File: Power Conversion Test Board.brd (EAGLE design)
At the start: 136.7 x 125.3 mm, 49 parts, among them U1 LM2678, U2 LM2678

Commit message: minor changes
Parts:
- added U$11, U$12, U$6: ET60S, ET60S:ET60S
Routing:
- net +3.3V: track 38.8 -> 28.8 mm, vias 1 -> 0
- net +5V: track 133.5 -> 136.1 mm
- net 3.3VGND: track 186.6 -> 188.2 mm
- net +12V: track 142.7 -> 143.5 mm
- net 5VGND: track 103.2 -> 103.4 mm, vias 7 -> 6
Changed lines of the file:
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@@
 </element>
 <element name="U$2" library="PDB_PCB_connectors" package="PDB_PCB_2" value="PDB_PCB_CONNEC" x="0" y="0"/>
+<element name="U$6" library="ET60S" package="ET60S" value="ET60S" x="40.3606" y="36.6776" rot="R120"/>
+<element name="U$11" library="ET60S" package="ET60S" value="ET60S" x="108.4072" y="57.7088" rot="R240"/>
+<element name="U$12" library="ET60S" package="ET60S" value="ET60S" x="56.1848" y="106.0958"/>
 </elements>
 <signals>
@@
 <wire x1="76.282" y1="56.642" x2="75.858" y2="57.066" width="1.27" layer="16"/>
 <wire x1="70.104" y1="69.596" x2="68.326" y2="71.374" width="1.27" layer="1"/>
-<wire x1="49.022" y1="71.374" x2="49.022" y2="68.834" width="1.143" layer="1"/>
 <wire x1="49.784" y1="68.072" x2="49.784" y2="66.548" width="1.143" layer="16"/>
 <wire x1="51.054" y1="65.278" x2="49.784" y2="66.548" width="1.143" layer="16"/>
@@
 <contactref element="U$2" pad="+12V14"/>
 <contactref element="U$2" pad="+12V44"/>
+<wire x1="49.022" y1="68.834" x2="48.1076" y2="69.7484" width="1.016" layer="1"/>
+<wire x1="48.1076" y1="70.4596" x2="49.022" y2="71.374" width="1.016" layer="1"/>
+<wire x1="48.1076" y1="69.7484" x2="48.1076" y2="70.4596" width="1.016" layer="1"/>
 <wire x1="93.446040625" y1="116.670159375" x2="95.9860375" y2="116.670159375" width="0" layer="19" extent="1-1"/>
 <wire x1="95.9860375" y1="114.1301625" x2="95.9860375" y2="116.670159375" width="0" layer="19" extent="1-1"/>
@@
 <contactref element="J6" pad="P$1"/>
 <wire x1="65.614" y1="97.962" x2="65.614" y2="94.234" width="1.27" layer="1"/>
-<wire x1="63.754" y1="99.822" x2="33.528" y2="99.822" width="1.27" layer="1"/>
-<wire x1="33.528" y1="99.822" x2="24.13" y2="109.22" width="1.27" layer="1"/>
-<wire x1="24.13" y1="110.744" x2="24.13" y2="109.22" width="1.27" layer="1"/>
-<wire x1="65.614" y1="97.962" x2="63.754" y2="99.822" width="1.27" layer="1"/>
 <wire x1="65.614" y1="94.234" x2="65.614" y2="88.392" width="1.27" layer="1"/>
 <wire x1="65.614" y1="88.392" x2="65.614" y2="82.55" width="1.27" layer="1"/>
@@
 <wire x1="46.736" y1="64.77" x2="46.736" y2="64.516" width="1.143" layer="16"/>
 <wire x1="54.864" y1="56.388" x2="46.736" y2="64.516" width="1.143" layer="16"/>
+<wire x1="24.13" y1="110.744" x2="34.7472" y2="100.1268" width="2.54" layer="1"/>
+<wire x1="65.614" y1="97.5556" x2="65.614" y2="94.234" width="2.54" layer="1"/>
+<wire x1="34.7472" y1="100.1268" x2="63.0428" y2="100.1268" width="2.54" layer="1"/>
+<wire x1="63.0428" y1="100.1268" x2="65.614" y2="97.5556" width="2.54" layer="1"/>
 </signal>
 <signal name="N$1">
@@
 <wire x1="56.642" y1="25.146" x2="49.022" y2="17.526" width="1.143" layer="16"/>
 <wire x1="49.022" y1="17.526" x2="49.022" y2="13.97" width="1.143" layer="16"/>
-<wire x1="69.85" y1="28.829" x2="69.85" y2="21.844" width="1.143" layer="1"/>
-<via x="69.85" y="28.829" extent="1-16" drill="0.6"/>
-<wire x1="69.85" y1="28.829" x2="69.547" y2="29.132" width="1.143" layer="16"/>
-<wire x1="69.547" y1="29.132" x2="67.024" y2="29.132" width="1.143" layer="16"/>
 </signal>
 <signal name="N$2">
@@
 <wire x1="94.0562" y1="64.3128" x2="99.008" y2="69.2646" width="0.889" layer="16"/>
 <wire x1="99.008" y1="74.168" x2="99.008" y2="77.2148" width="0.889" layer="16"/>
-<wire x1="101.766" y1="79.9728" x2="101.766" y2="88.138" width="0.889" layer="16"/>
-<wire x1="99.008" y1="77.2148" x2="101.766" y2="79.9728" width="0.889" layer="16"/>
+<wire x1="99.008" y1="77.2148" x2="102.362" y2="80.5688" width="1.016" layer="16"/>
+<wire x1="102.362" y1="87.542" x2="101.766" y2="88.138" width="1.016" layer="16"/>
+<wire x1="102.362" y1="80.5688" x2="102.362" y2="87.542" width="1.016" layer="16"/>
 </signal>
 <signal name="3.3VGND">
@@
 <wire x1="91.7448" y1="78.74" x2="93.091" y2="80.0862" width="0.889" layer="16"/>
 <via x="93.091" y="80.0862" extent="1-16" drill="0.6"/>
-<wire x1="93.091" y1="80.0862" x2="93.7142" y2="80.0862" width="0.889" layer="1"/>
-<wire x1="93.7142" y1="80.0862" x2="101.702" y2="88.074" width="0.889" layer="1"/>
 <wire x1="106.188" y1="76.453" x2="106.188" y2="87.3346" width="0.889" layer="16"/>
 <wire x1="106.188" y1="87.3346" x2="105.6132" y2="87.9094" width="0.889" layer="16"/>
@@
 <wire x1="105.6132" y1="87.9094" x2="105.4486" y2="88.074" width="0.889" layer="1"/>
 <wire x1="105.4486" y1="88.074" x2="101.702" y2="88.074" width="0.889" layer="1"/>
+<wire x1="93.091" y1="80.0862" x2="96.9264" y2="83.9216" width="1.016" layer="1"/>
+<wire x1="101.8286" y1="85.4964" x2="101.8286" y2="88.0246" width="1.016" layer="1"/>
+<wire x1="96.9264" y1="83.9216" x2="100.2538" y2="83.9216" width="1.016" layer="1"/>
+<wire x1="100.2538" y1="83.9216" x2="101.8286" y2="85.4964" width="1.016" layer="1"/>
 </signal>
 <signal name="N$10">
@@
 <contactref element="C9" pad="-"/>
 <contactref element="C1" pad="-"/>
-<wire x1="51.562" y1="96.774" x2="51.562" y2="93.726" width="1.143" layer="1"/>
+<wire x1="51.562" y1="96.774" x2="51.562" y2="96.3422" width="1.143" layer="1"/>
+<wire x1="51.562" y1="96.3422" x2="51.562" y2="93.726" width="1.143" layer="1"/>
 <wire x1="51.562" y1="93.726" x2="51.562" y2="88.646" width="1.143" layer="1"/>
 <wire x1="51.562" y1="88.646" x2="51.562" y2="86.995" width="1.143" layer="1"/>
@@
 <wire x1="63.246" y1="57.15" x2="58.42" y2="52.324" width="1.143" layer="1"/>
 <wire x1="58.42" y1="52.324" x2="58.42" y2="47.244" width="1.143" layer="1"/>
-<wire x1="33.274" y1="118.618" x2="33.274" y2="104.14" width="1.143" layer="16"/>
-<wire x1="49.276" y1="97.79" x2="39.624" y2="97.79" width="1.143" layer="16"/>
-<via x="49.276" y="97.79" extent="1-16" drill="0.6"/>
-<wire x1="50.546" y1="97.79" x2="49.276" y2="97.79" width="1.143" layer="1"/>
-<wire x1="51.562" y1="96.774" x2="50.546" y2="97.79" width="1.143" layer="1"/>
-<wire x1="39.624" y1="97.79" x2="33.274" y2="104.14" width="1.143" layer="16"/>
 <wire x1="56.134" y1="71.374" x2="56.134" y2="60.96" width="1.016" layer="16"/>
 <wire x1="56.388" y1="60.706" x2="56.134" y2="60.96" width="1.016" layer="16"/>
@@
 <wire x1="66.708" y1="45.028" x2="66.708" y2="41.142" width="1.27" layer="16"/>
 <wire x1="66.708" y1="41.142" x2="66.548" y2="40.982" width="1.27" layer="16"/>
+<wire x1="33.274" y1="118.618" x2="33.274" y2="103.2002" width="2.54" layer="16"/>
+<wire x1="33.274" y1="103.2002" x2="38.5318" y2="97.9424" width="2.54" layer="16"/>
+<wire x1="38.5318" y1="97.9424" x2="49.9872" y2="97.9424" width="2.54" layer="16"/>
+<wire x1="49.9872" y1="97.9424" x2="51.2318" y2="96.6978" width="2.54" layer="16"/>
 <wire x1="60.759975" y1="45.212" x2="66.708" y2="45.028" width="0" layer="19" extent="1-16"/>
 </signal>

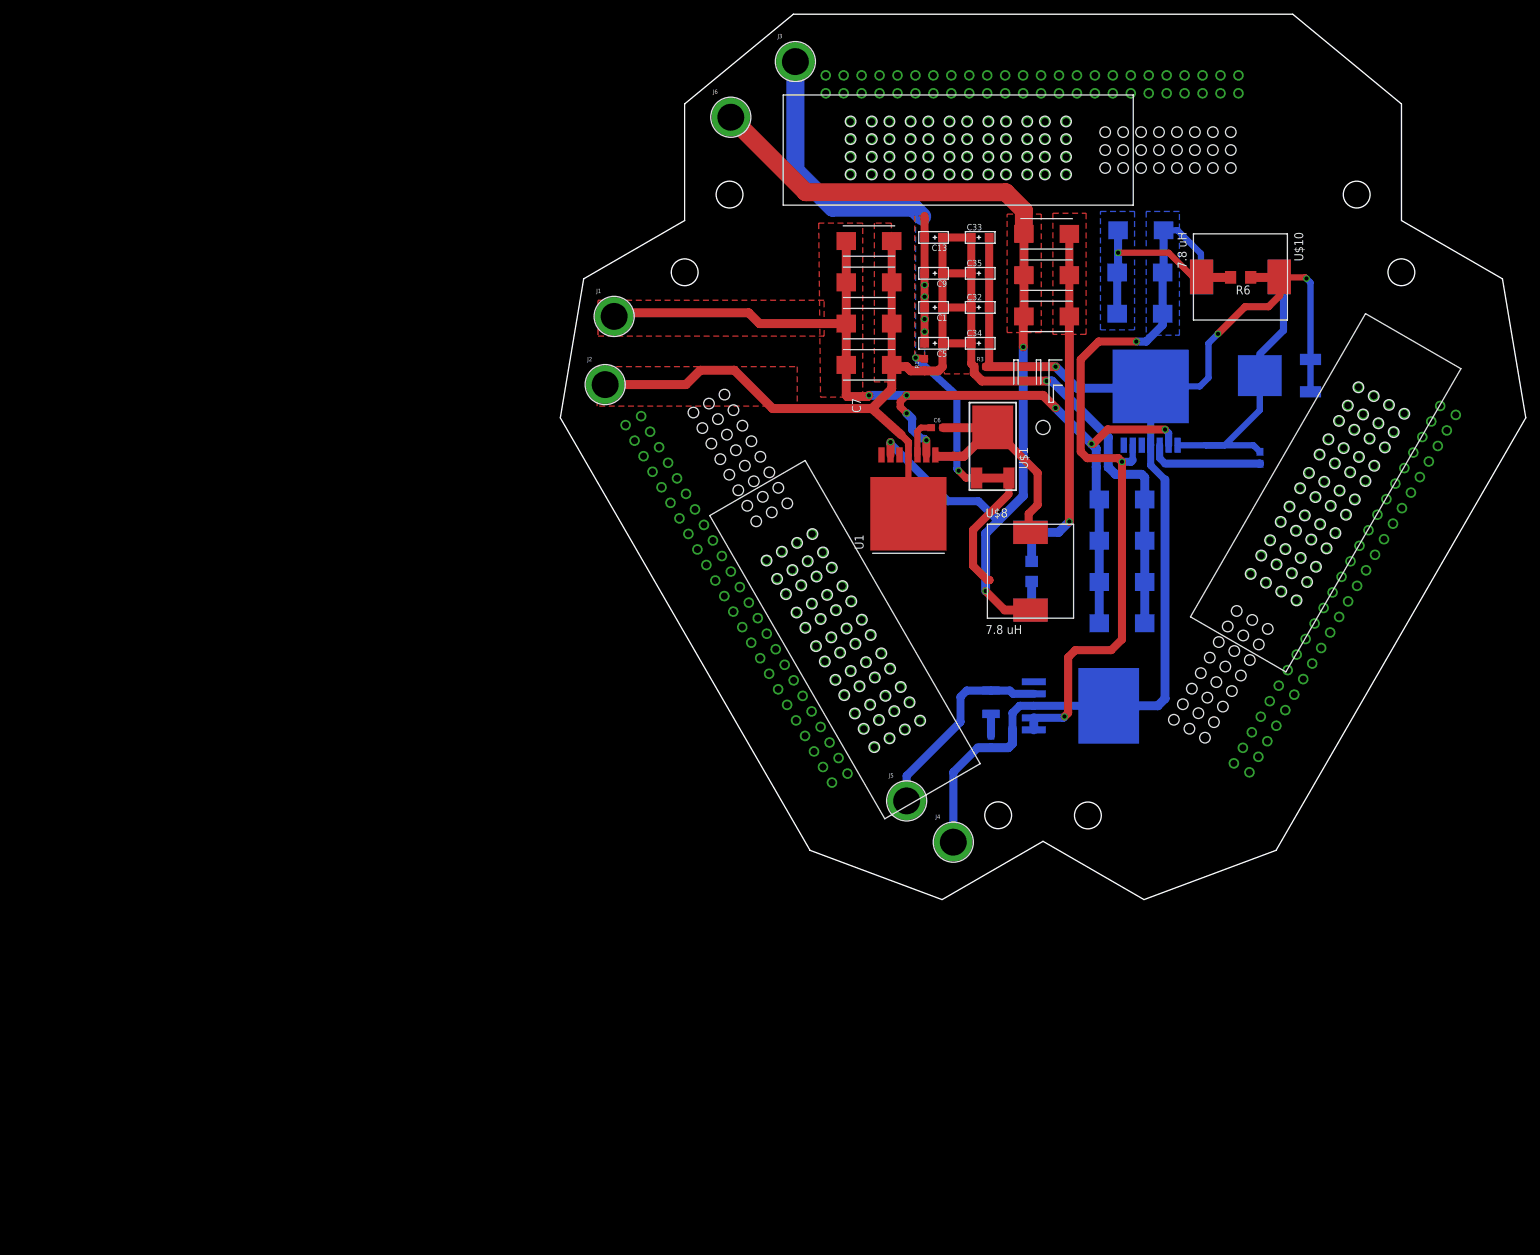
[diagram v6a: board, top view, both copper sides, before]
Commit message: Netted connectors
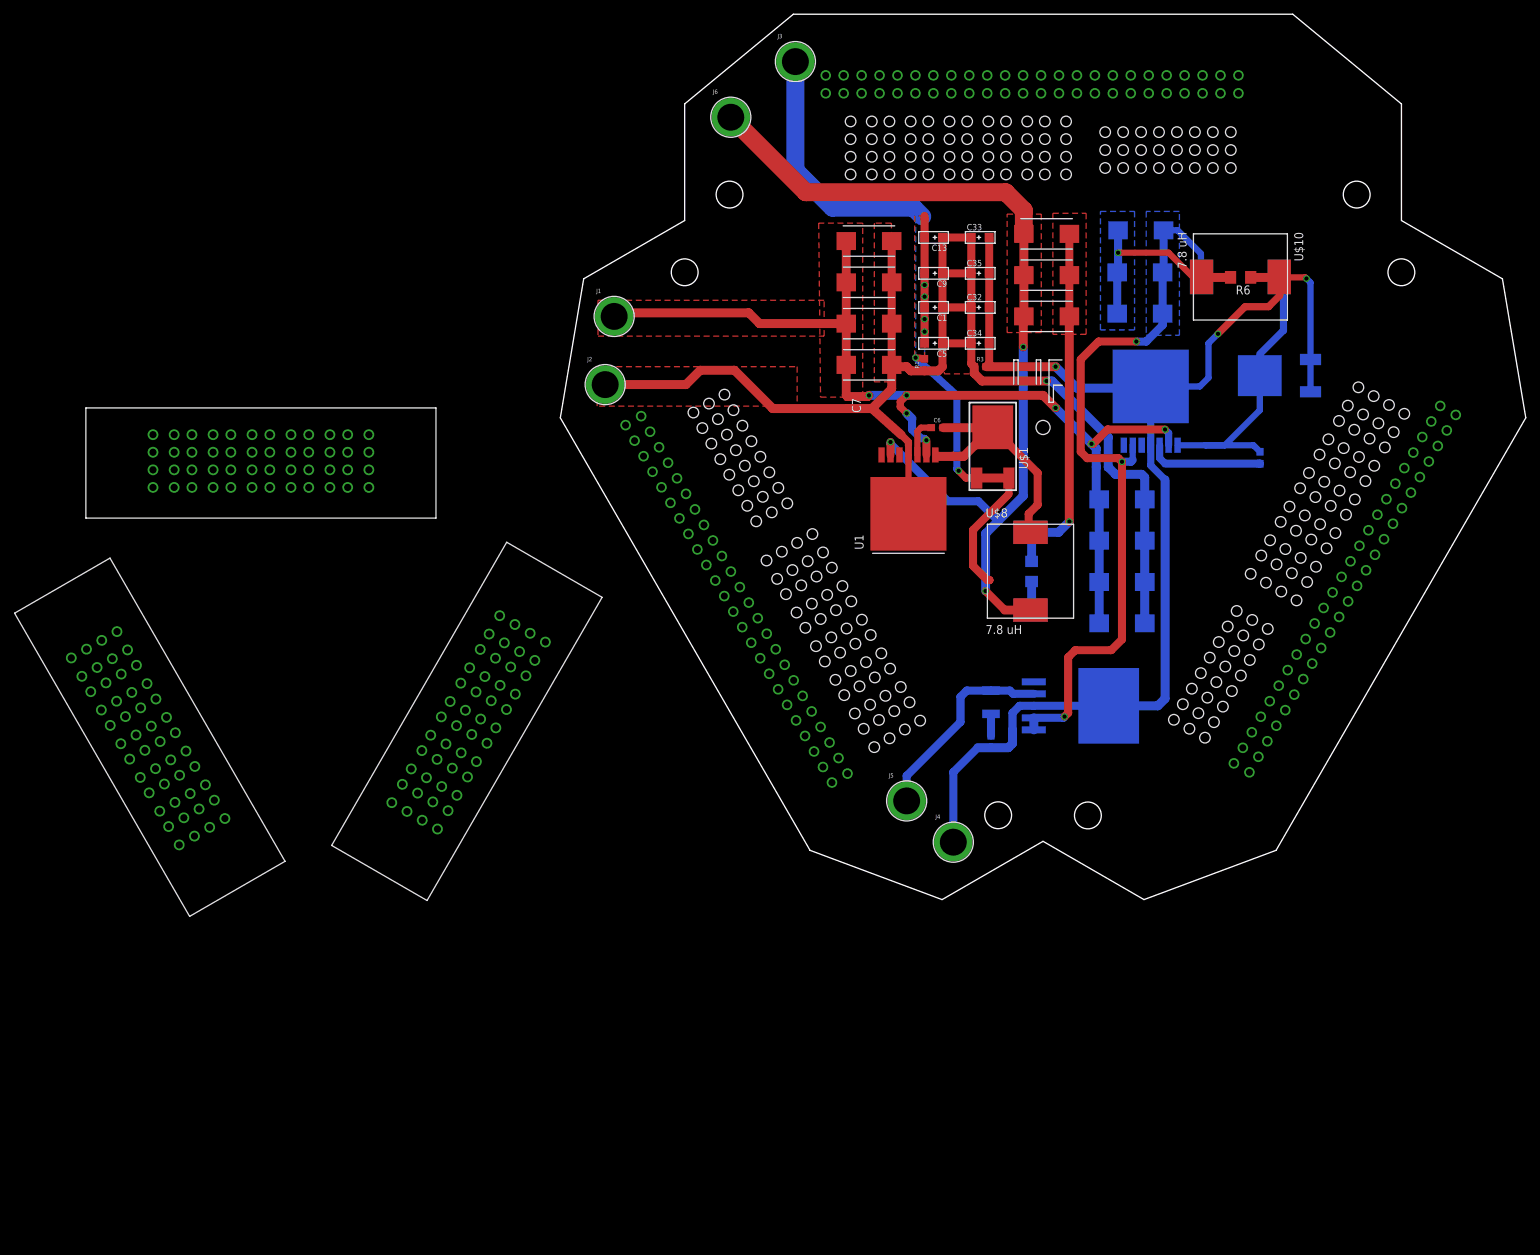
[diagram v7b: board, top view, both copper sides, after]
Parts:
- moved U$11 125.8 mm to (-13.2, 25.3)
- moved U$12 108.2 mm to (-42.5, 61.8)
- moved U$6 99.4 mm to (-58.0, 22.9)
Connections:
- net +12V: now also U$11.P$58, U$11.P$59, U$11.P$64, U$11.P$65, U$11.P$66, U$11.P$67, U$11.P$72, U$11.P$73, U$12.P$58, U$12.P$59, U$12.P$64, U$12.P$65, U$12.P$66, U$12.P$67, U$12.P$72, U$12.P$73, U$6.P$58, U$6.P$59, U$6.P$64, U$6.P$65, U$6.P$66, U$6.P$67, U$6.P$72, U$6.P$73
- net +3.3V: now also U$11.P$60, U$11.P$61, U$11.P$62, U$11.P$63, U$11.P$68, U$11.P$69, U$11.P$70, U$11.P$71, U$12.P$60, U$12.P$61, U$12.P$62, U$12.P$63, U$12.P$68, U$12.P$69, U$12.P$70, U$12.P$71, U$6.P$60, U$6.P$61, U$6.P$62, U$6.P$63, U$6.P$68, U$6.P$69, U$6.P$70, U$6.P$71
- net +5V: now also U$11.P$41, U$11.P$42, U$11.P$43, U$11.P$44, U$11.P$45, U$11.P$46, U$11.P$47, U$11.P$48, U$12.P$41, U$12.P$42, U$12.P$43, U$12.P$44, U$12.P$45, U$12.P$46, U$12.P$47, U$12.P$48, U$6.P$41, U$6.P$42, U$6.P$43, U$6.P$44, U$6.P$45, U$6.P$46, U$6.P$47, U$6.P$48
- net 3.3VGND: now also U$11.P$25, U$11.P$26, U$11.P$27, U$11.P$28, U$11.P$29, U$11.P$30, U$11.P$31, U$11.P$32, U$12.P$25, U$12.P$26, U$12.P$27, U$12.P$28, U$12.P$29, U$12.P$30, U$12.P$31, U$12.P$32, U$6.P$25, U$6.P$26, U$6.P$27, U$6.P$28, U$6.P$29, U$6.P$30, U$6.P$31, U$6.P$32
- net 5VGND: now also U$11.P$49, U$11.P$50, U$11.P$51, U$11.P$52, U$11.P$53, U$11.P$54, U$11.P$55, U$11.P$56, U$12.P$49, U$12.P$50, U$12.P$51, U$12.P$52, U$12.P$53, U$12.P$54, U$12.P$55, U$12.P$56, U$6.P$49, U$6.P$50, U$6.P$51, U$6.P$52, U$6.P$53, U$6.P$54, U$6.P$55, U$6.P$56
- net GND: now also U$11.P$33, U$11.P$34, U$11.P$35, U$11.P$36, U$11.P$37, U$11.P$38, U$11.P$39, U$11.P$40, U$12.P$33, U$12.P$34, U$12.P$35, U$12.P$36, U$12.P$37, U$12.P$38, U$12.P$39, U$12.P$40, U$6.P$33, U$6.P$34, U$6.P$35, U$6.P$36, U$6.P$37, U$6.P$38, U$6.P$39, U$6.P$40

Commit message: small tweak on connectors
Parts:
- moved U$12 119.2 mm to (68.2, 106.1)
- moved U$11 117.6 mm to (102.4, 47.3)
- moved U$6 95.5 mm to (34.4, 47.1)
